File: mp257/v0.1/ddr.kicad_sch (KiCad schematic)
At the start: 70 parts, among them U6 STM32MP257FAK3, U7 MT40A1G16TB-062E IT:F

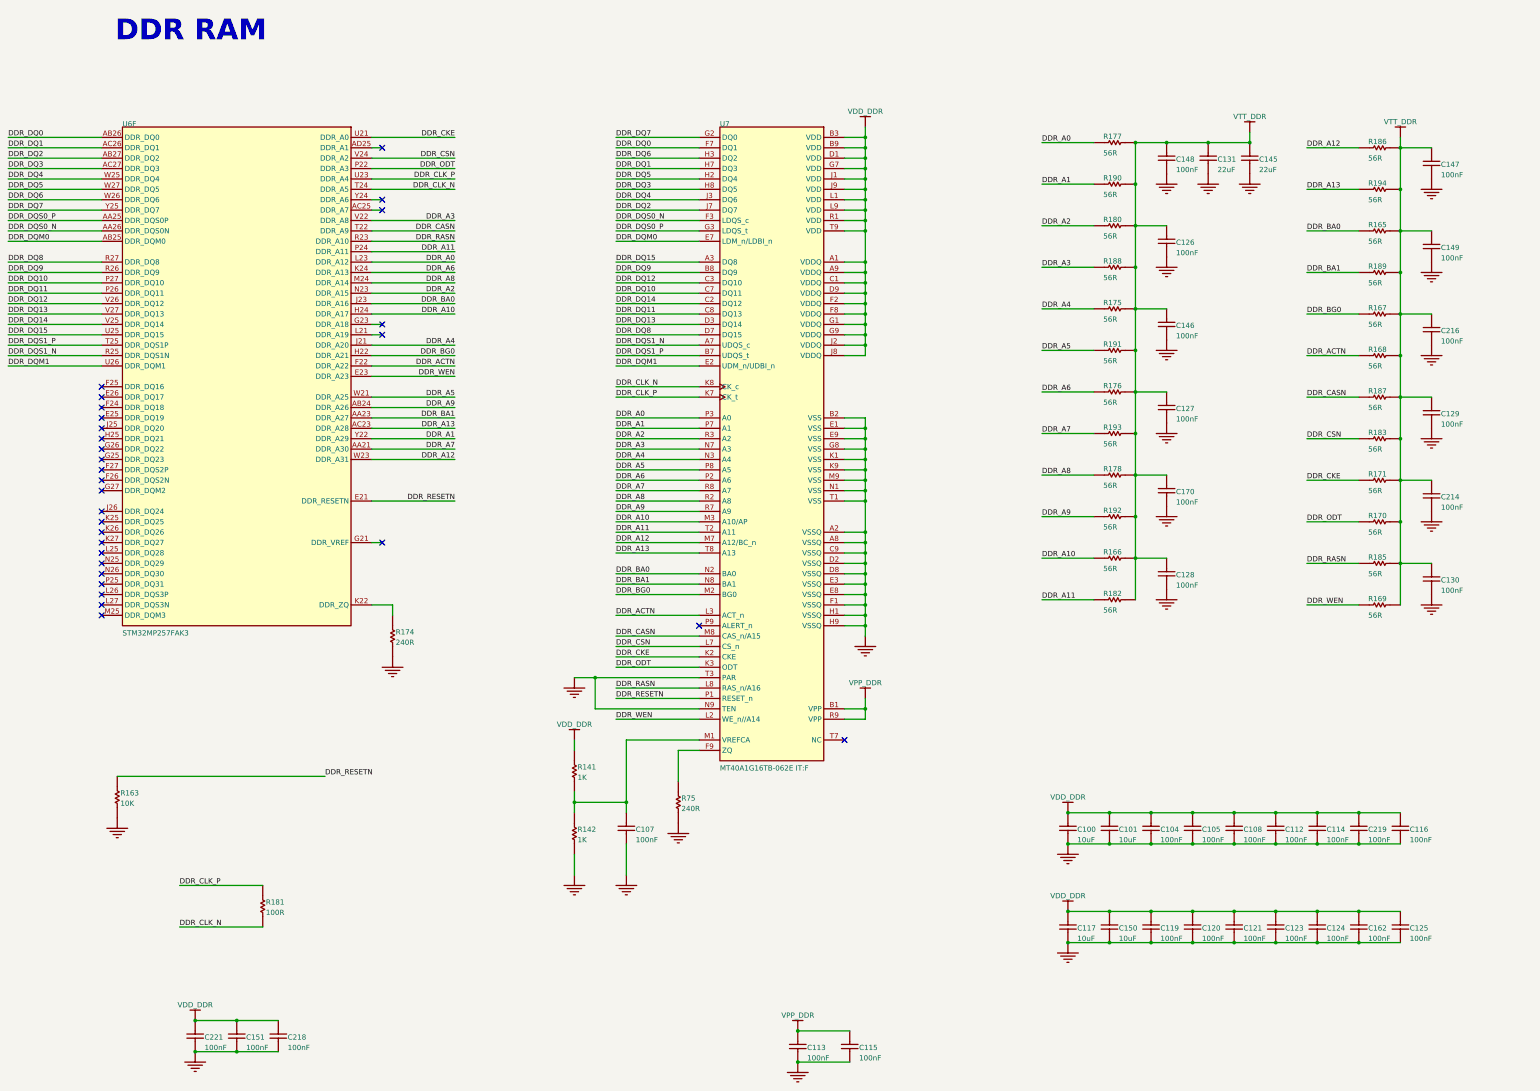
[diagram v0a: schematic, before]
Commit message: Fix ref nums pasted from reference schematic
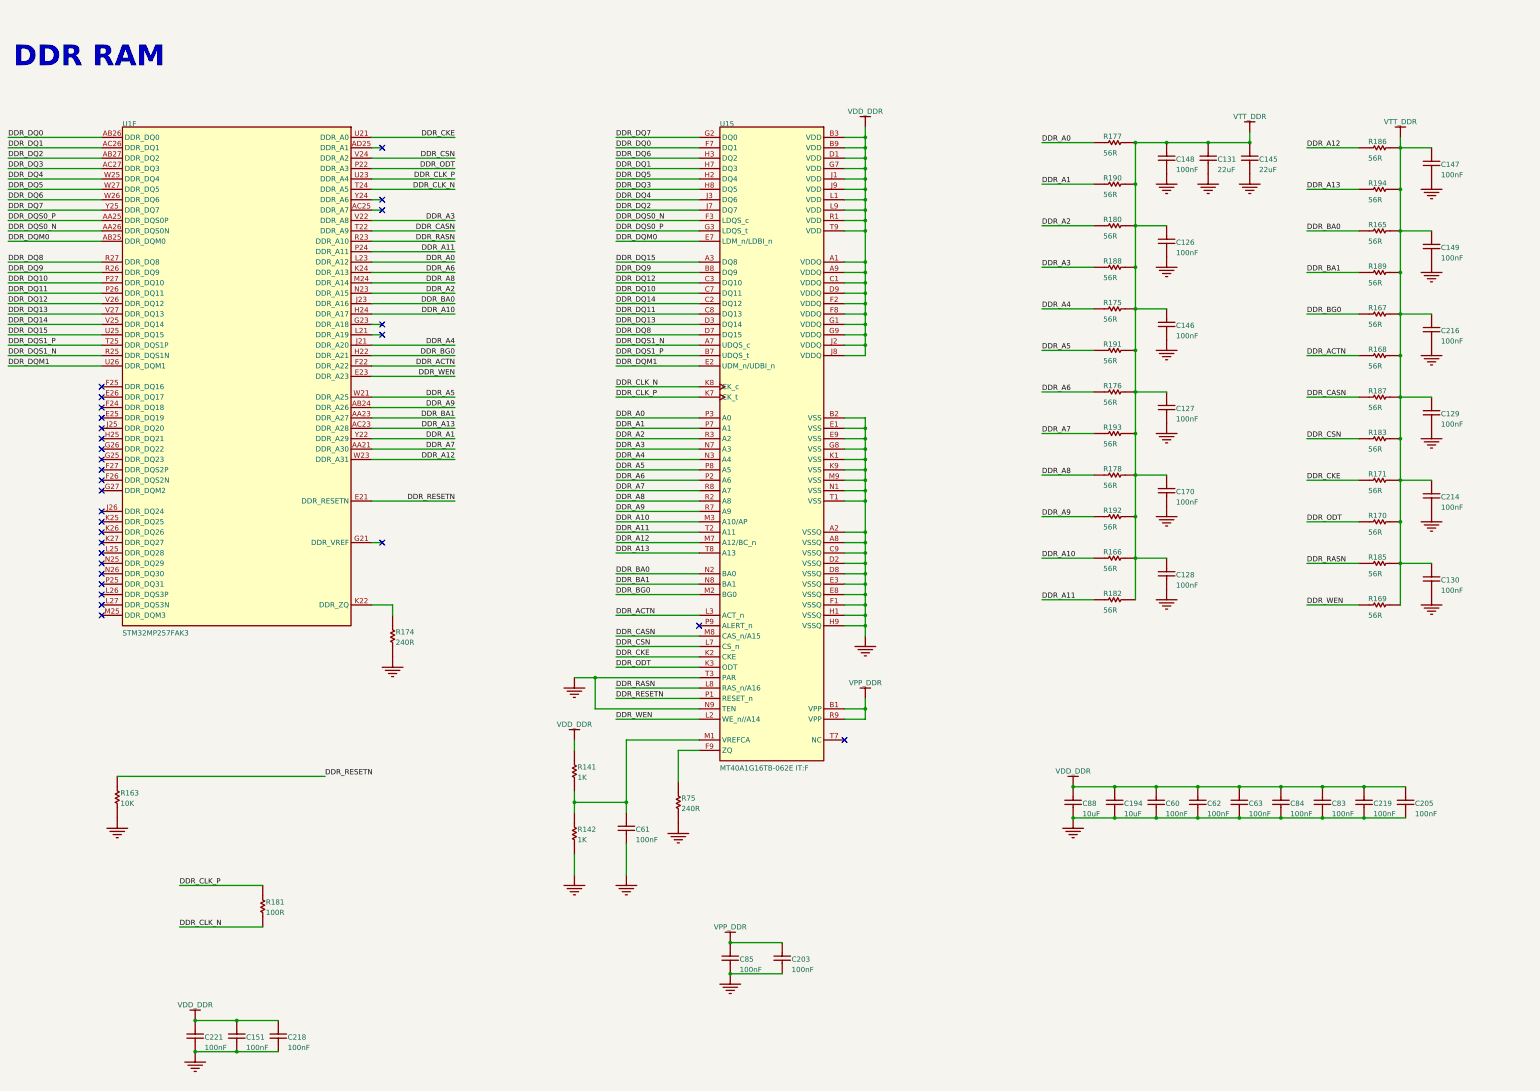
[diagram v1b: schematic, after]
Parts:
- removed C100, C101, C117, C150: Capacitor, C0603, symbol MCD_PARTS_database:U_2_DDR4_16bits_1_Capacitor_MCD_PARTS_database.DbLib
- removed C104, C105, C108, C112, C114, C116, C119, C120, C121, C123, C124, C125, C162: Capacitor, C0402, symbol MCD_PARTS_database:U_2_DDR4_16bits_1_Capacitor_MCD_PARTS_database.DbLib
- added C194, C88: Capacitor, C0603, symbol MCD_PARTS_database:U_2_DDR4_16bits_1_Capacitor_MCD_PARTS_database.DbLib
- added C205, C60, C62, C63, C83, C84: Capacitor, C0402, symbol MCD_PARTS_database:U_2_DDR4_16bits_1_Capacitor_MCD_PARTS_database.DbLib
- renumbered C115 to C203, C107 to C61, C113 to C85, U6 to U1, U7 to U15
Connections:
- net GND: now also C194.1, C205.1, C60.1, C62.1, C63.1, C83.1, C84.1, C88.1
- net VDD_DDR: now also C194.2, C205.2, C60.2, C62.2, C63.2, C83.2, C84.2, C88.2
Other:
- moved on the sheet: C203, C85

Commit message: WIP: symbols
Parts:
- U1: symbol MCD_PARTS_database:U_2_DDR4_16bits_0_STM32MP257FAK3_MCD_PARTS_database.DbLib -> 4ms_IC:STM32MP257FAKx

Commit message: Updated RAM and STM32MP2 footprints to 4ms lib
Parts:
- U1: footprint ICC_TFBGA424_14X14_P050_H1P20_CODE-B0A2 -> 4ms_Package_QFP:TFBGA-424_14x14mm_P0.5_STM_AK
- U15: footprint ICC_FBGA96_TB_7P5X13_P080 -> 4ms_Package_QFP:FBGA-96_Layout2x3x16_Body8x14_P0.8mm

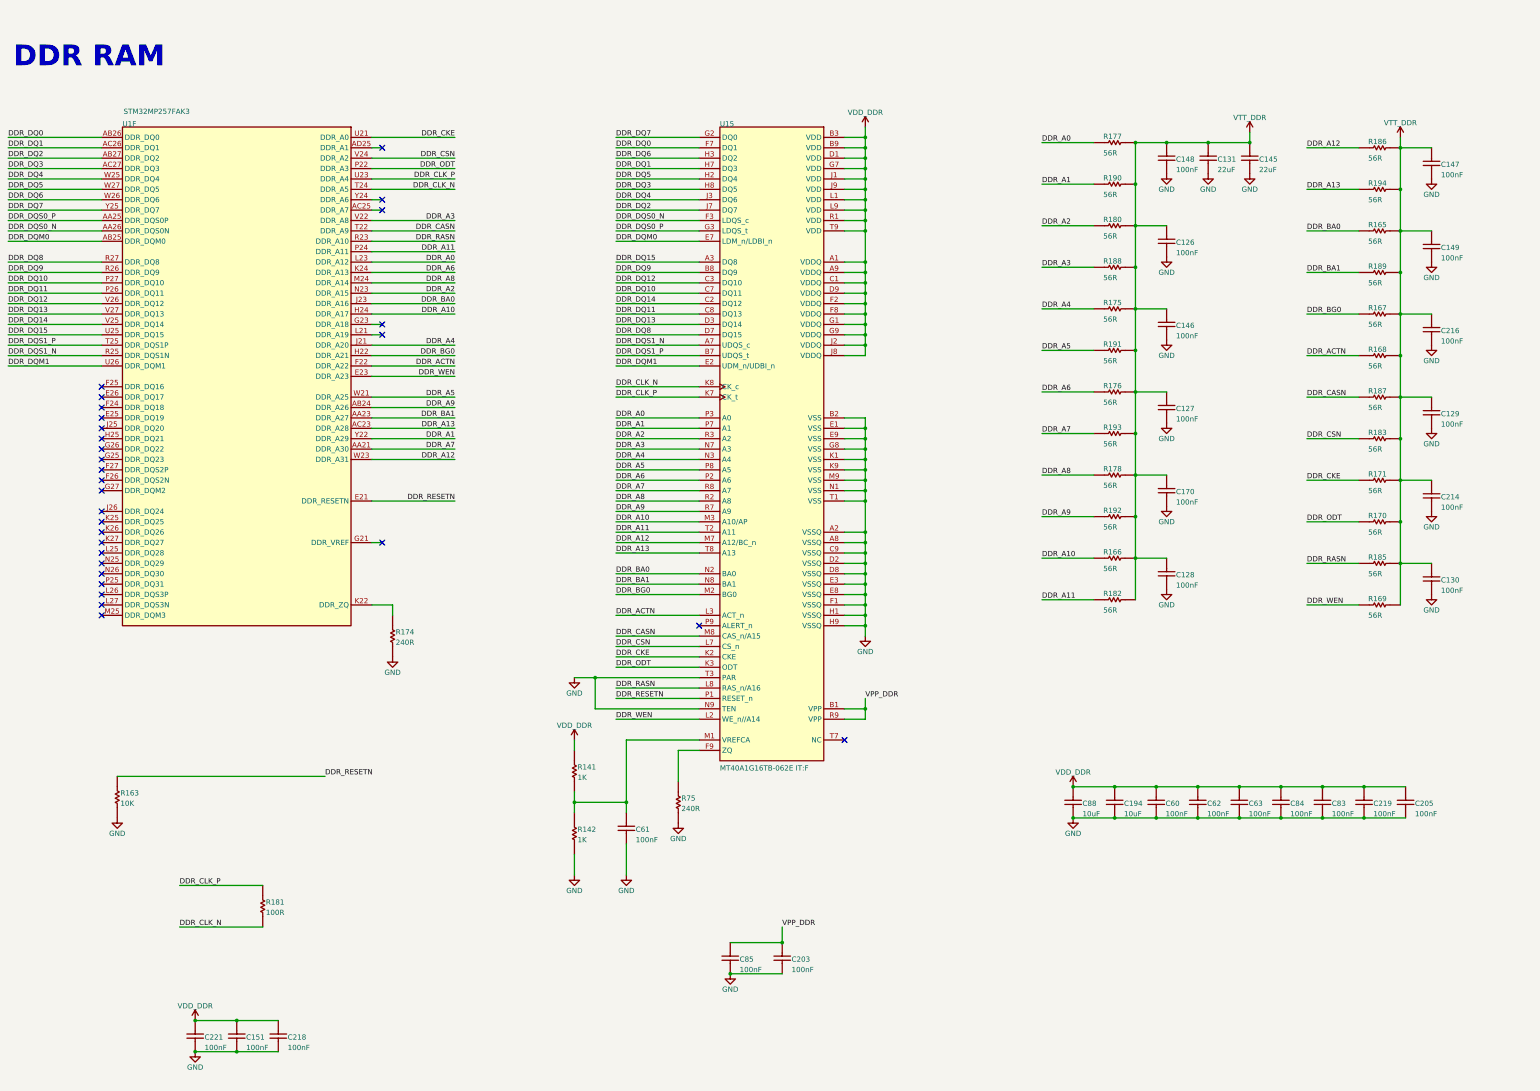
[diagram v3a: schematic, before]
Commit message: Updating parts to 4ms lib
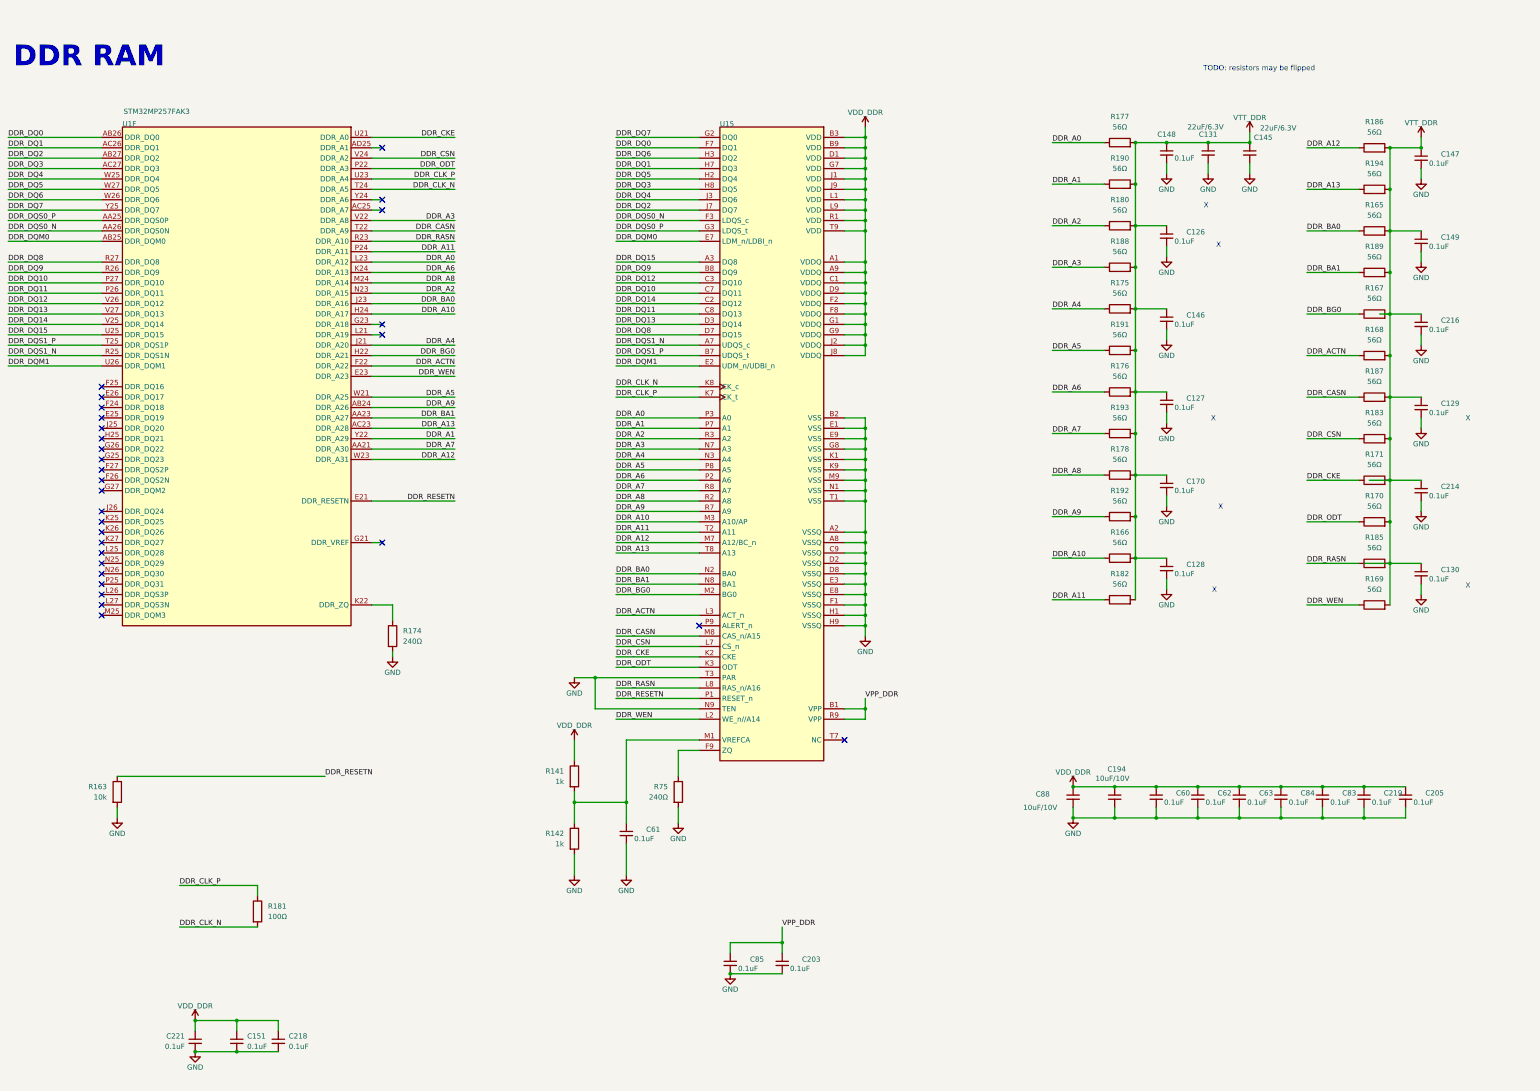
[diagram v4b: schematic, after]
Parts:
- C126, C127, C128, C129, C130, C146, C147, C148, C149, C151, C170, C203, C205, C214, C216, C218, C219, C221, C60, C61, C62, C63, C83, C84, C85: value Capacitor -> 100nF_0402_16V; footprint C0402 -> 4ms_Capacitor:C_0402; symbol MCD_PARTS_database:U_2_DDR4_16bits_1_Capacitor_MCD_PARTS_database.DbLib -> 4ms_Capacitor:100nF_0402_16V; ALTERNATE_MANUFACTURER MURATA -> (none); ALTERNATE_MANUFACTURER_PART_NUMBER GCM155R71C104KA55D -> (none); ALTIUM_VALUE 100nF -> (none); COMPONENTLINK1DESCRIPTION Datasheet -> (none); COMPONENTLINK1URL http://tunmcdsvn.tun.st.com/Component_Documentation_Library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 -> (none); Display (none) -> 0.1uF; INTERNAL_PART_NUMBER MCD-00006 -> (none); JLCPCB ID (none) -> C1525; MANUFACTURER YAGEO -> (none); MANUFACTURER_PART_NUMBER CC0402KRX7R7BB104 -> (none); Manufacturer (none) -> Murata; Manufacturer 2 (none) -> Yageo; ORDER_CODE_DIGIKEY 311-1338-1-ND -> (none); ORDER_CODE_FARNELL 9402047 -> (none); ORDER_CODE_RS 616-9701 -> (none); PACKAGE 0402 -> (none); PART_PREFERENCE Recommended -> (none); PART_TYPE Capacitor -> (none); Part Number (none) -> GCM155R71C104KA55D; Part Number 2 (none) -> CC0402KRX7R7BB104; Production Stage (none) -> A; STATUS Released -> (none); Specifications (none) -> 0.1uF, Min. 16V 10%, X7R or X5R or similar
- C131, C145: value Capacitor -> 22uF_0603_6.3V; footprint C0603 -> 4ms_Capacitor:C_0603; symbol MCD_PARTS_database:U_2_DDR4_16bits_1_Capacitor_MCD_PARTS_database.DbLib -> 4ms_Capacitor:22uF_0603_6.3V; ALTERNATE_MANUFACTURER N/A -> (none); ALTERNATE_MANUFACTURER_PART_NUMBER N/A -> (none); ALTIUM_VALUE 22uF -> (none); COMPONENTLINK1DESCRIPTION Datasheet -> (none); COMPONENTLINK1URL http://tunmcdsvn.tun.st.com/Component_Documentation_Library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 -> (none); Display (none) -> 22uF/6.3V; INTERNAL_PART_NUMBER MCD-00100 -> (none); JLCPCB ID (none) -> C59461; MANUFACTURER MURATA -> (none); MANUFACTURER_PART_NUMBER GRM188R60J226MEA0J -> (none); Manufacturer (none) -> Murata; ORDER_CODE_DIGIKEY 490-7612-2-ND -> (none); ORDER_CODE_FARNELL N/A -> (none); ORDER_CODE_RS N/A -> (none); PACKAGE 0603 -> (none); PART_PREFERENCE Recommended -> (none); PART_TYPE Capacitor -> (none); Part Number (none) -> GRM188R60J226MEA0J; Production Stage (none) -> A; STATUS Released -> (none); Specifications (none) -> 22uF, 6.3V,10%,X5R or X7R,0603
- C194, C88: value Capacitor -> 10uF_0603_10V; footprint C0603 -> 4ms_Capacitor:C_0603; symbol MCD_PARTS_database:U_2_DDR4_16bits_1_Capacitor_MCD_PARTS_database.DbLib -> 4ms_Capacitor:10uF_0603_10V; ALTERNATE_MANUFACTURER MURATA -> (none); ALTERNATE_MANUFACTURER_PART_NUMBER GRM188R60J106ME84D -> (none); ALTIUM_VALUE 10uF -> (none); COMPONENTLINK1URL http://tunmcdsvn.tun.st.com/Component_Documentation_Library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 -> (none); Display (none) -> 10uF/10V; INTERNAL_PART_NUMBER MCD-01341 -> (none); JLCPCB ID (none) -> C19702; MANUFACTURER MURATA -> (none); MANUFACTURER_PART_NUMBER GRM188R60J106ME47D -> (none); Manufacturer (none) -> Murata; ORDER_CODE_DIGIKEY 490-3896-1-ND -> (none); ORDER_CODE_FARNELL 1735528 -> (none); ORDER_CODE_RS N/A -> (none); PACKAGE 0603 -> (none); PART_PREFERENCE Recommended -> (none); PART_TYPE Capacitor -> (none); Part Number (none) -> GRM188R61A106KE69D; Production Stage (none) -> A; STATUS Released -> (none); Specifications (none) -> 10uF, Min. 10V X5R 10%
- R141, R142: value Resistor -> 1k_0402; footprint R0402 -> 4ms_Resistor:R_0402; symbol MCD_PARTS_database:U_2_DDR4_16bits_1_Resistor_MCD_PARTS_database.DbLib -> 4ms_Resistor_0402:1k_0402; ALTIUM_VALUE 1K -> (none); COMPONENTLINK1URL http://tunmcdsvn.tun.st.com/Component_Documentation_Library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 -> (none); COMPONENT_COUNTRY_OF_ORIGIN China -> (none); Display (none) -> 1k; ID 2532 -> (none); INTERNAL_PART_NUMBER MCD-00061 -> (none); JLCPCB ID (none) -> C106235; MANUFACTURER YAGEO -> (none); MANUFACTURER_PART_NUMBER RC0402FR-071KL -> (none); Manufacturer (none) -> Yageo; ORDER_CODE_DIGIKEY 311-1.00KLRCT-ND -> (none); ORDER_CODE_FARNELL 9239235 -> (none); ORDER_CODE_RS 9239235 -> (none); PACKAGE 0402 -> (none); PART_PREFERENCE Recommended -> (none); PART_TYPE Resistor -> (none); Part Number (none) -> RC0402FR-071KL; Production Stage (none) -> A; SHOWFIELDS YES -> (none); STATUS Released -> (none); Specifications (none) -> 1k, 1%, 1/16W, 0402
- R163: value Resistor -> 10k_0402; footprint R0402 -> 4ms_Resistor:R_0402; symbol MCD_PARTS_database:U_2_DDR4_16bits_1_Resistor_MCD_PARTS_database.DbLib -> 4ms_Resistor_0402:10k_0402; ALTERNATE_MANUFACTURER N/A -> (none); ALTERNATE_MANUFACTURER_PART_NUMBER N/A -> (none); ALTIUM_VALUE 10K -> (none); BMS_PART_NUMBER 9131590 -> (none); COMPONENTLINK1DESCRIPTION Datasheet -> (none); COMPONENTLINK1URL http://tunmcdsvn.tun.st.com/Component_Documentation_Library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 -> (none); Display (none) -> 10k; INTERNAL_PART_NUMBER MCD-00053 -> (none); JLCPCB ID (none) -> C60490; MANUFACTURER YAGEO -> (none); MANUFACTURER_PART_NUMBER RC0402FR-0710KL -> (none); Manufacturer (none) -> Yageo; ORDER_CODE_DIGIKEY 311-10.0KLRCT-ND -> (none); ORDER_CODE_FARNELL 9239359 -> (none); ORDER_CODE_RS N/A -> (none); PACKAGE 0402 -> (none); PART_PREFERENCE Recommended -> (none); PART_TYPE Resistor -> (none); Part Number (none) -> RC0402FR-0710KL; Production Stage (none) -> A; STATUS Released -> (none); Specifications (none) -> 10k, 1%, 1/16W, 0402
- R165, R166, R167, R168, R169, R170, R171, R175, R176, R177, R178, R180, R182, R183, R185, R186, R187, R188, R189, R190, R191, R192, R193, R194: value Resistor -> 56Ω_0402; footprint R0402 -> 4ms_Resistor:R_0402; symbol MCD_PARTS_database:U_2_DDR4_16bits_0_Resistor_MCD_PARTS_database.DbLib -> 4ms_Resistor_0402:56Ω_0402; ALTERNATE_MANUFACTURER N/A -> (none); ALTERNATE_MANUFACTURER_PART_NUMBER N/A -> (none); ALTIUM_VALUE 56R -> (none); COMPONENTLINK1URL http://tunmcdsvn.tun.st.com/Component_Documentation_Library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 -> (none); Display (none) -> 56Ω; INTERNAL_PART_NUMBER MCD-00054 -> (none); JLCPCB ID (none) -> C137957; MANUFACTURER YAGEO -> (none); MANUFACTURER_PART_NUMBER RC0402FR-0756RL -> (none); Manufacturer (none) -> Yageo; ORDER_CODE_DIGIKEY 311-56.0LRCT-ND -> (none); ORDER_CODE_FARNELL 9239081 -> (none); ORDER_CODE_RS N/A -> (none); PACKAGE 0402 -> (none); PART_PREFERENCE Recommended -> (none); PART_TYPE Resistor -> (none); Part Number (none) -> RC0402FR-0756RL; Production Stage (none) -> A; STATUS Released -> (none); Specifications (none) -> 56Ω, 1%, 1/16W, 0402
- R174, R75: value Resistor -> 240Ω_0402; footprint R0201_H0P23 -> 4ms_Resistor:R_0402; symbol MCD_PARTS_database:U_2_DDR4_16bits_1_Resistor_MCD_PARTS_database.DbLib -> 4ms_Resistor_0402:240Ω_0402; ALTERNATE_MANUFACTURER N/A -> (none); ALTERNATE_MANUFACTURER_PART_NUMBER N/A -> (none); ALTIUM_VALUE 240R -> (none); COMPONENTLINK1URL http://tunmcdsvn.tun.st.com/Component_Datasheet_Library/Tru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 -> (none); Display (none) -> 240Ω; INTERNAL_PART_NUMBER MCD-02253 -> (none); JLCPCB ID (none) -> C114755; MANUFACTURER YAGEO -> (none); MANUFACTURER_PART_NUMBER RC0201FR-07240RL -> (none); Manufacturer (none) -> Yageo; ORDER_CODE_DIGIKEY YAG2528CT-ND -> (none); ORDER_CODE_FARNELL N/A -> (none); ORDER_CODE_RS N/A -> (none); PACKAGE R0201 -> (none); PART_PREFERENCE Recommended -> (none); PART_TYPE Resistor -> (none); Part Number (none) -> RC0402FR-07240RL; Production Stage (none) -> A; STATUS Checked -> (none); Specifications (none) -> 240Ω, 1%, 1/16W, 0402
- R181: value Resistor -> 100Ω_0402; footprint R0402 -> 4ms_Resistor:R_0402; symbol MCD_PARTS_database:U_2_DDR4_16bits_3_Resistor_MCD_PARTS_database.DbLib -> 4ms_Resistor_0402:100Ω_0402; ALTERNATE_MANUFACTURER N/A -> (none); ALTERNATE_MANUFACTURER_PART_NUMBER N/A -> (none); ALTIUM_VALUE 100R -> (none); COMPONENTLINK1DESCRIPTION Datasheet -> (none); COMPONENTLINK1URL http://tunmcdsvn.tun.st.com/Component_Documentation_Library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 -> (none); Display (none) -> 100Ω; INTERNAL_PART_NUMBER MCD-01819 -> (none); JLCPCB ID (none) -> C106232; MANUFACTURER YAGEO -> (none); MANUFACTURER_PART_NUMBER RC0402DR-07100RL -> (none); Manufacturer (none) -> Yageo; ORDER_CODE_DIGIKEY RC0402DR-07100RL-ND -> (none); ORDER_CODE_FARNELL N/A -> (none); ORDER_CODE_RS N/A -> (none); PACKAGE 0402 -> (none); PART_PREFERENCE Recommended -> (none); PART_TYPE Resistor -> (none); Part Number (none) -> RC0402FR-07100RL; Production Stage (none) -> A; STATUS Released -> (none); Specifications (none) -> 100Ω, 1%, 1/16W, 0402
- U15: symbol MCD_PARTS_database:U_2_DDR4_16bits_0_MT40A1G16TB-062E IT{colon}F_MCD_PARTS_database.DbLib -> 4ms_IC:DDR4-RAM-16Gbit-MT40A1G16TB-062E; ALTIUM_VALUE MT40A1G16TB-062E IT:F -> (none); COMPONENTLINK1URL http://tunmcdsvn.tun.st.com/Component_Documentation_Library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 -> (none); COMPONENT_COUNTRY_OF_ORIGIN Taiwan° -> (none); ID 5639 -> (none); INTERNAL_PART_NUMBER MCD-03523 -> (none); MANUFACTURER MICRON -> (none); MANUFACTURER_PART_NUMBER MT40A1G16TB-062E IT:F -> (none); Manufacturer (none) -> MICRON; ORDER_CODE_DIGIKEY N/A -> (none); ORDER_CODE_FARNELL N/A -> (none); ORDER_CODE_RS N/A -> (none); PACKAGE FBGA-96 -> (none); PART_PREFERENCE Recommended -> (none); PART_TYPE IC -> (none); Part Number (none) -> MT40A1G16TB-062E IT:F; SHOWFIELDS YES -> (none); STATUS Checked -> (none)
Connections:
- net DDR_RESETN: now also R163.1; no longer R163.2
- net GND: now also C126.2, C127.2, C128.2, C129.2, C130.2, C131.2, C145.2, C146.2, C147.2, C148.2, C149.2, C151.2, C170.2, C194.2, C203.2, C205.2, C214.2, C216.2, C218.2, C219.2, C221.2, C60.2, C61.2, C62.2, C63.2, C83.2, C84.2, C85.2, C88.2, R142.2, R163.2, R174.2, R75.2; no longer C126.1, C127.1, C128.1, C129.1, C130.1, C131.1, C145.1, C146.1, C147.1, C148.1, C149.1, C151.1, C170.1, C194.1, C203.1, C205.1, C214.1, C216.1, C218.1, C219.1, C221.1, C60.1, C61.1, C62.1, C63.1, C83.1, C84.1, C85.1, C88.1, R142.1, R163.1, R174.1, R75.1
- net VDD_DDR: now also C151.1, C194.1, C205.1, C218.1, C219.1, C221.1, C60.1, C62.1, C63.1, C83.1, C84.1, C88.1, R141.1; no longer C151.2, C194.2, C205.2, C218.2, C219.2, C221.2, C60.2, C62.2, C63.2, C83.2, C84.2, C88.2, R141.2
- net VPP_DDR: now also C203.1, C85.1; no longer C203.2, C85.2
- net VTT_DDR: now also C126.1, C127.1, C128.1, C129.1, C130.1, C131.1, C145.1, C146.1, C147.1, C148.1, C149.1, C170.1, C214.1, C216.1; no longer C126.2, C127.2, C128.2, C129.2, C130.2, C131.2, C145.2, C146.2, C147.2, C148.2, C149.2, C170.2, C214.2, C216.2
- net at U1.K22 (DDR_ZQ): now also R174.1; no longer R174.2
- net at U15.F9 (ZQ): now also R75.1; no longer R75.2
- new net: C61.1, R141.2, R142.1, U15.M1 (VREFCA)
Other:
- note added: "TODO: resistors may be flipped"
- note added: "X"
- moved on the sheet: R141, R142, R163, R165, R166, R167, R168, R169, R170, R171, R175, R176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

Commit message: WIP
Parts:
- renumbered C214 to C146, C170 to C212, C127 to C213, C146 to C214, C126 to C215
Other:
- moved on the sheet: C128, C129, C146, C147, C148, C149, C212, C213, C214, C215, C216
